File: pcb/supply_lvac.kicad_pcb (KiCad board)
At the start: 2 copper layers, 203.2 x 35.6 mm, 50 parts, among them J1 Barrel_Jack, J2 Conn_01x10, J3 Conn_01x10, J4 Conn_01x10, J5 Conn_01x10, J6 Conn_01x10, J7 Conn_01x10, J8 Conn_01x10, J9 Conn_01x10, U1 L7812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

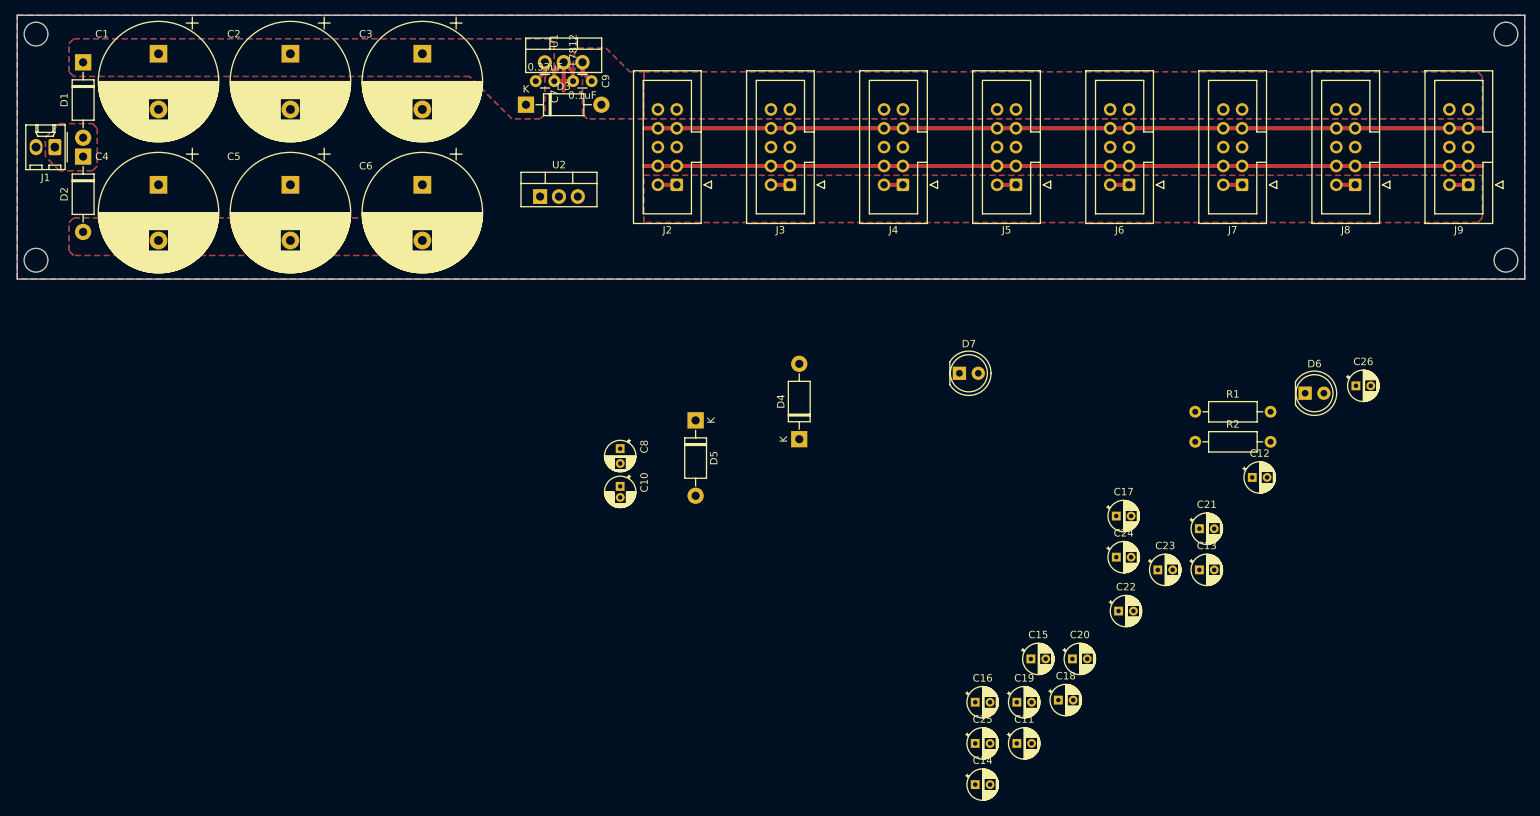
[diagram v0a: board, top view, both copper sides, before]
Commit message: Start via stitching
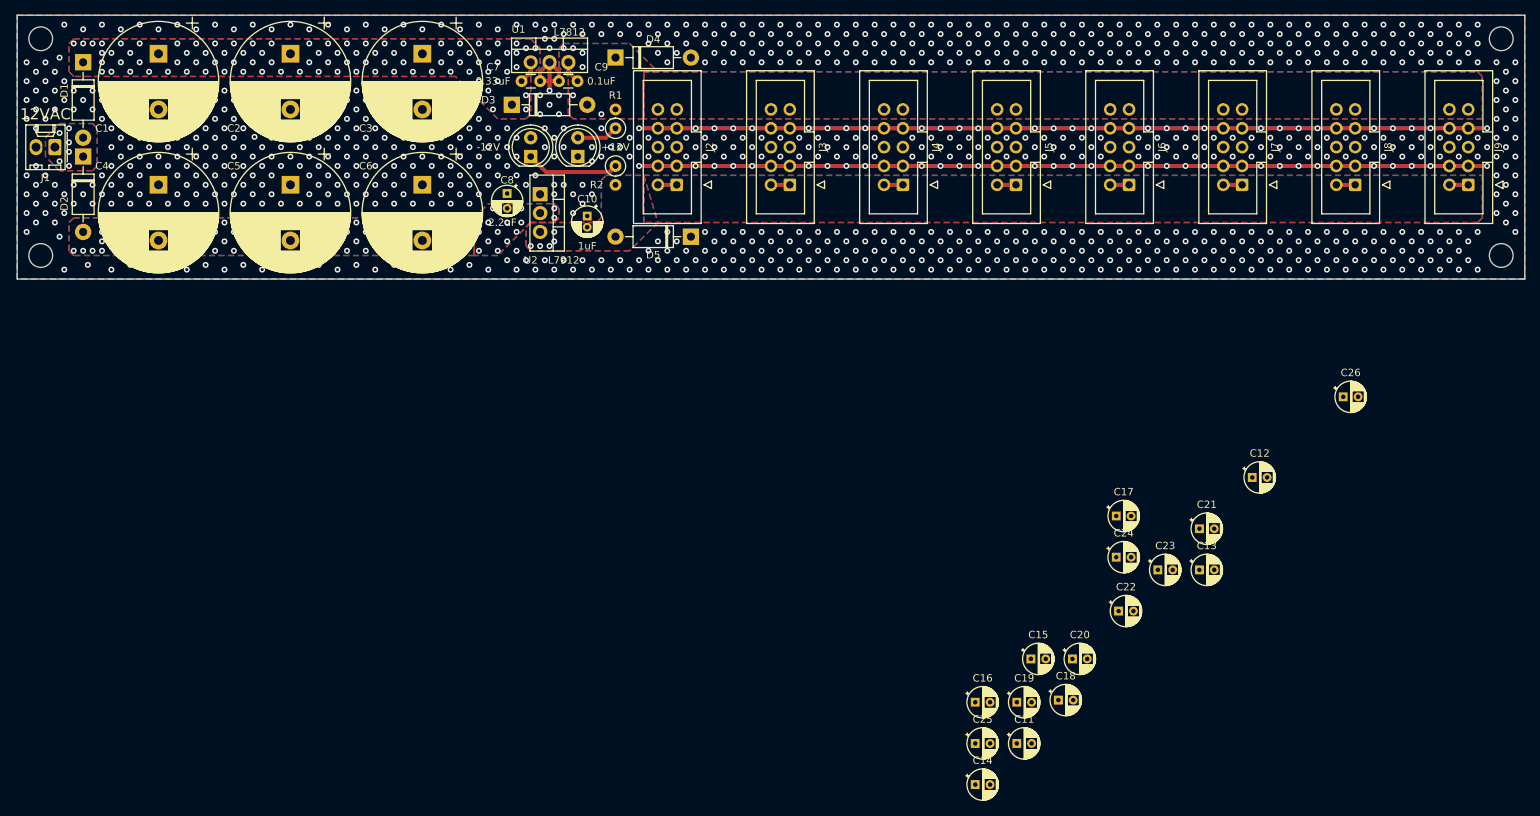
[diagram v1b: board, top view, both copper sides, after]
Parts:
- R1, R2: footprint Resistor_THT:R_Axial_DIN0207_L6.3mm_D2.5mm_P10.16mm_Horizontal -> Resistor_THT:R_Axial_DIN0207_L6.3mm_D2.5mm_P2.54mm_Vertical
- moved D6 103.1 mm to (123.8, 57.1), turned to 90 degrees
- moved R1 87.0 mm to (128.9, 53.3), turned to 90 degrees
- moved R2 86.5 mm to (128.9, 58.4), turned to -90 degrees
- moved D7 64.7 mm to (117.5, 57.2), turned to 90 degrees
- moved D4 57.1 mm to (128.9, 43.8), turned to 0 degrees
- moved C8 37.6 mm to (114.3, 62.1)
- moved C10 36.7 mm to (125.1, 65.2)
- moved D5 24.8 mm to (139.1, 67.9), turned to 180 degrees
- moved C26 2.26 mm to (227.0, 89.5)
- moved C7 1.91 mm to (118.7, 47.0)
- moved C9 1.91 mm to (123.8, 47.0)
- moved D3 1.91 mm to (114.9, 50.2)
- moved U1 1.91 mm to (117.5, 44.5)
- moved H2 0.90 mm to (51.4, 70.5)
- moved H1 0.90 mm to (51.4, 41.3)
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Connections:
- D6 pad 1: Net-(D6-Pad1) -> GND
- D6 pad 2: +12V -> Net-(R1-Pad1)
- D7 pad 1: -12V -> Net-(D7-Pad1)
- D7 pad 2: Net-(D7-Pad2) -> GND
- R1 pad 1: Net-(D6-Pad1) -> Net-(R1-Pad1)
- R1 pad 2: GND -> +12V
- R2 pad 1: GND -> Net-(D7-Pad1)
- R2 pad 2: Net-(D7-Pad2) -> -12V
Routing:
- net Net-(D7-Pad1): track 0.00 -> 12.6 mm
- net Net-(R1-Pad1): track 0.00 -> 5.61 mm
- net GND: vias 0 -> 1048
- net /VREC-: vias 0 -> 87
- net /VREC+: vias 0 -> 92
- net /VAC: vias 0 -> 6
- net -12V: vias 0 -> 5
- net +12V: vias 0 -> 6
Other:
- board text added: "12VAC"

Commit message: Complete layout. Export gerbers
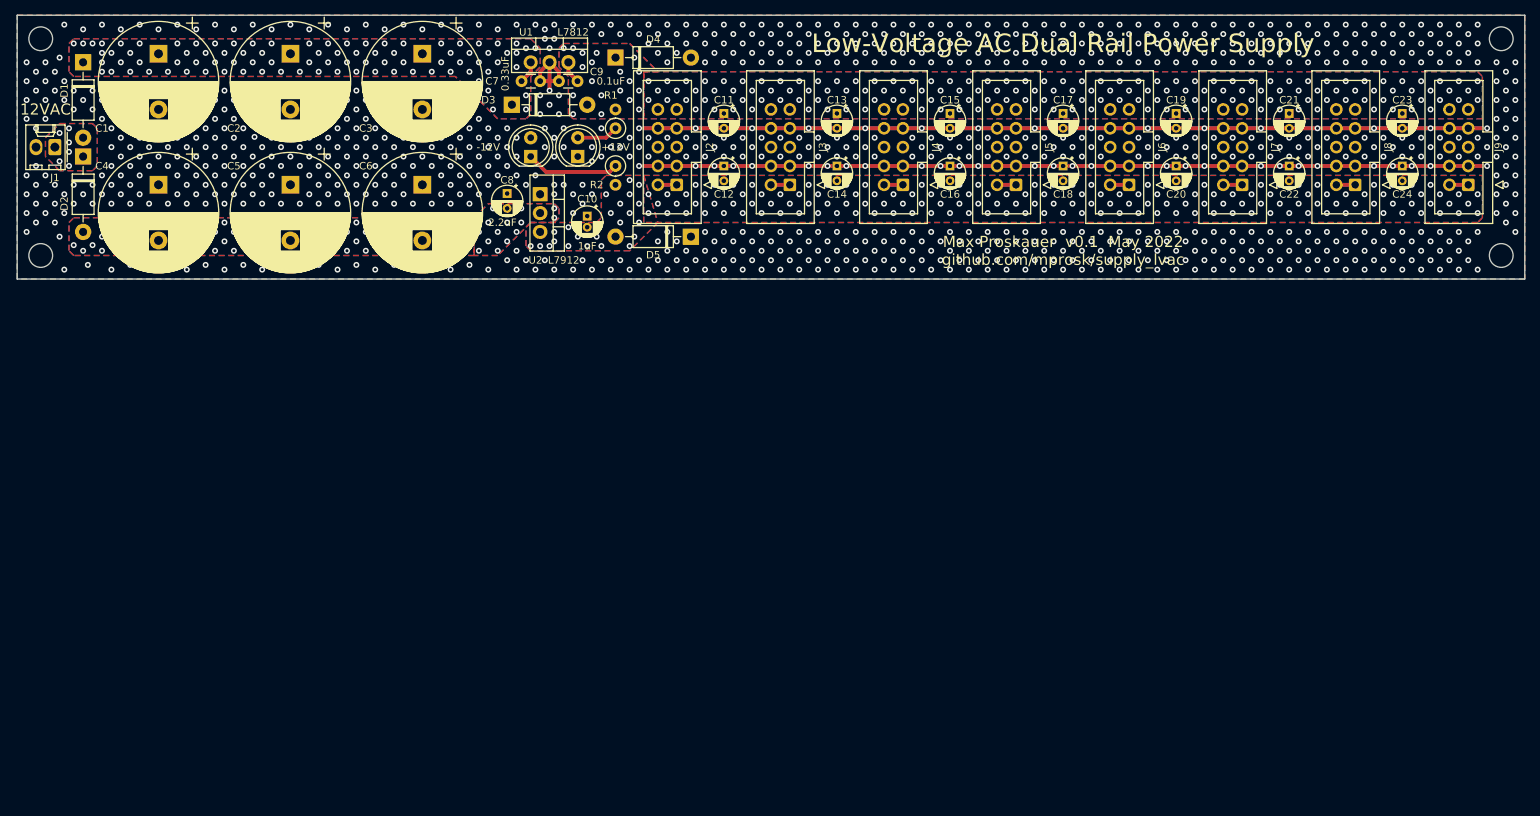
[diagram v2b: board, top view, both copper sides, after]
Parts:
- removed C25, C26: 100uF, Capacitor_THT:CP_Radial_D4.0mm_P2.00mm
- moved C11 93.6 mm to (143.5, 51.3), turned to -90 degrees
- moved C14 85.4 mm to (158.8, 58.4), turned to -90 degrees
- moved C12 82.7 mm to (143.5, 58.4), turned to -90 degrees
- moved C19 82.2 mm to (204.5, 51.3), turned to -90 degrees
- moved C13 78.6 mm to (158.8, 51.3), turned to -90 degrees
- moved C15 74.3 mm to (174.0, 51.3), turned to -90 degrees
- moved C16 72.4 mm to (174.0, 58.4), turned to -90 degrees
- moved C18 72.0 mm to (189.2, 58.4), turned to -90 degrees
- moved C23 69.8 mm to (234.9, 51.3), turned to -90 degrees
- moved C20 67.9 mm to (204.5, 58.4), turned to -90 degrees
- moved C24 65.3 mm to (234.9, 58.4), turned to -90 degrees
- moved C22 64.2 mm to (219.7, 58.4), turned to -90 degrees
- moved C21 57.3 mm to (219.7, 51.3), turned to -90 degrees
- moved C17 54.7 mm to (189.2, 51.3), turned to -90 degrees
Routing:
- net GND: vias 1048 -> 1042
- net /VREC-: vias 87 -> 86
- net /VREC+: vias 92 -> 90
- net -12V: vias 5 -> 178
- net +12V: vias 6 -> 174
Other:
- board text added: "JLCJLCJLCJLC"
- board text added: "Low-Voltage AC Dual Rail Power Supply"
- board text added: "Max Proskauer v0.1 May 2022 github.com/mprosk/supply_lvac"
